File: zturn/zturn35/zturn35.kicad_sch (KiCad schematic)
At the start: 58 parts, among them U1 74AXP4T245, U10 74AXP4T245, U11 74AXP4T245, U12 74AXP4T245, U2 74AXP4T245, U3 74AXP4T245, U4 74AXP4T245, U5 74AXP4T245, U6 74AXP4T245, U7 74AXP4T245, U8 74AXP4T245, U9 74AXP4T245

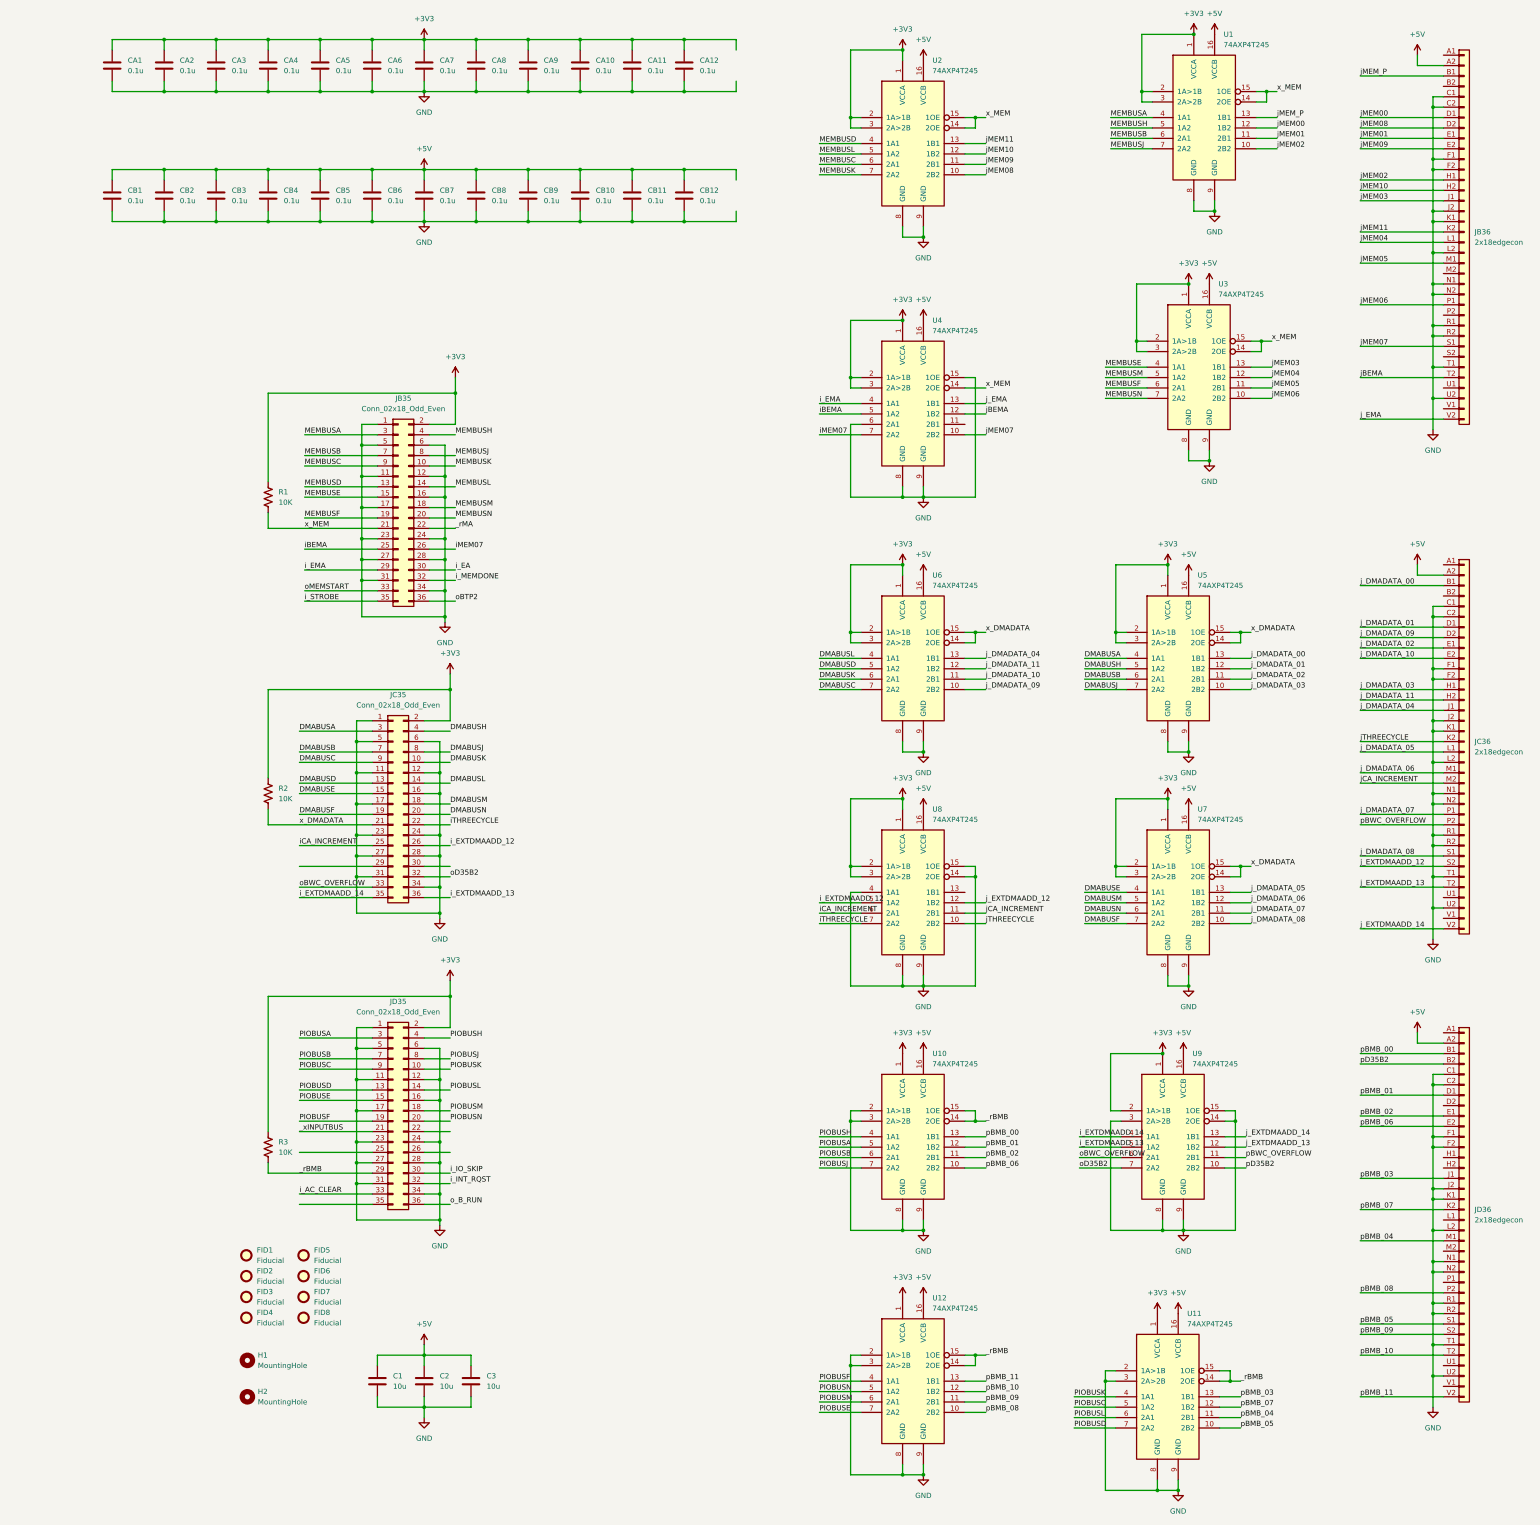
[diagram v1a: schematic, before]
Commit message: use transistors for bus drivers instead of chips
to handle the 180 & 220-ohm pullups
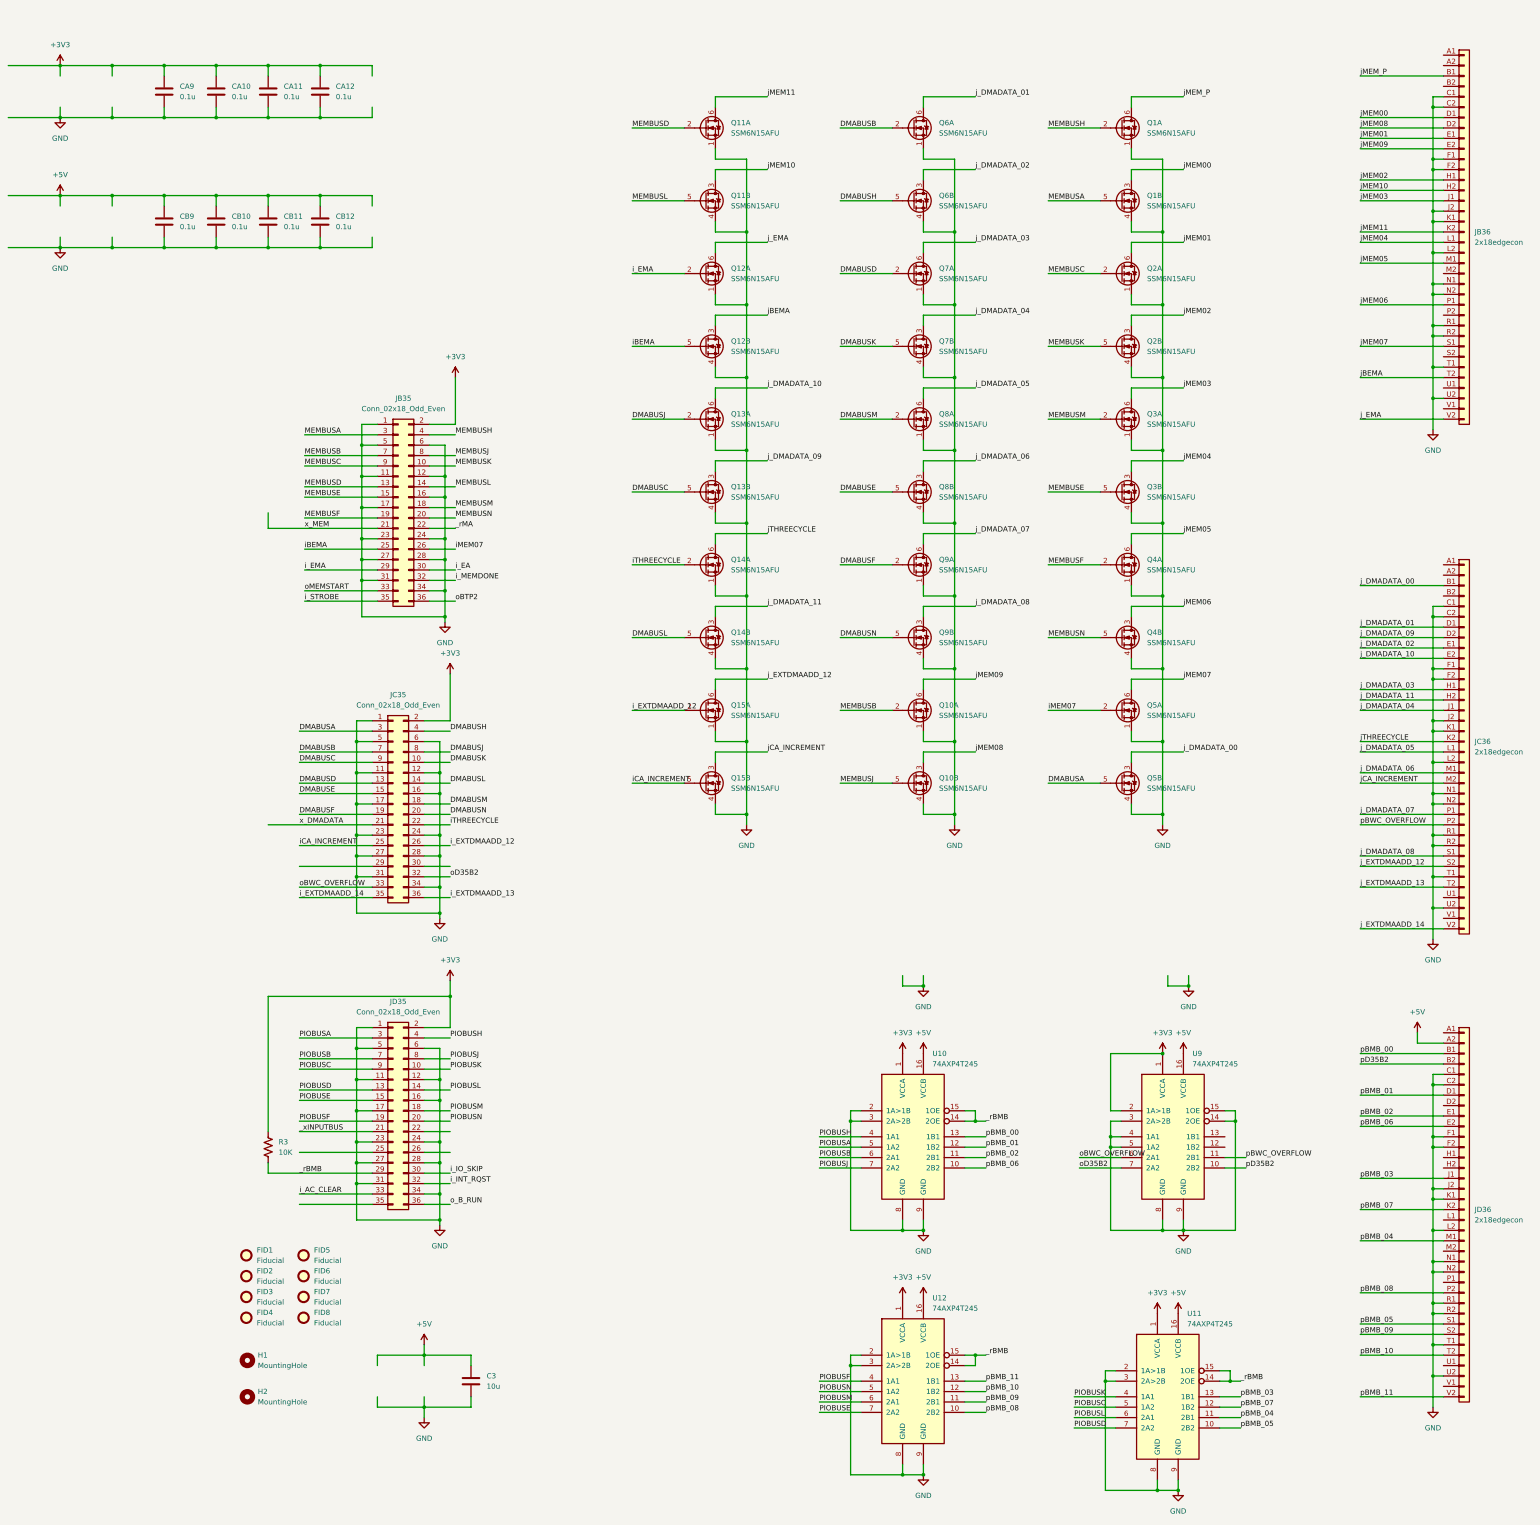
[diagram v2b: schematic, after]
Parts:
- removed C1, C2: 10u, Capacitor_SMD:C_1206_3216Metric, symbol Device:C
- removed CA1, CA2, CA3, CA4, CA5, CA6, CA7, CA8, CB1, CB2, CB3, CB4, CB5, CB6, CB7, CB8: 0.1u, Capacitor_SMD:C_0201_0603Metric, symbol Device:C
- removed R1, R2: 10K, Resistor_SMD:R_0201_0603Metric, symbol Device:R_US
- removed U1, U2, U3, U4, U5, U6, U7, U8: 74AXP4T245, Package_SO:TSSOP-16_4.4x5mm_P0.65mm, symbol mylibrary:74AXP4T245
- added Q1, Q10, Q11, Q12, Q13, Q14, Q15, Q2, Q3, Q4, Q5, Q6, Q7, Q8, Q9: SSM6N15AFU, Package_TO_SOT_SMD:SOT-363_SC-70-6, symbol mylibrary:SSM6N15AFU
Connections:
- net +5V: no longer JB36.A2, JC36.A2
- net DMABUSA: now also Q5.5 (G2)
- net DMABUSB: now also Q6.2 (G1)
- net DMABUSC: now also Q13.5 (G2)
- net DMABUSD: now also Q7.2 (G1)
- net DMABUSE: now also Q8.5 (G2)
- net DMABUSF: now also Q9.2 (G1)
- net DMABUSH: now also Q6.5 (G2)
- net DMABUSJ: now also Q13.2 (G1)
- net DMABUSK: now also Q7.5 (G2)
- net DMABUSL: now also Q14.5 (G2)
- net DMABUSM: now also Q8.2 (G1)
- net DMABUSN: now also Q9.5 (G2)
- net GND: now also U9.4 (1A1), U9.5 (1A2), Q1.1 (S1), Q1.4 (S2), Q10.1 (S1), Q10.4 (S2), Q11.1 (S1), Q11.4 (S2), Q12.1 (S1), Q12.4 (S2), Q13.1 (S1), Q13.4 (S2), Q14.1 (S1), Q14.4 (S2), Q15.1 (S1), Q15.4 (S2), Q2.1 (S1), Q2.4 (S2), Q3.1 (S1), Q3.4 (S2), Q4.1 (S1), Q4.4 (S2), Q5.1 (S1), Q5.4 (S2), Q6.1 (S1), Q6.4 (S2), Q7.1 (S1), Q7.4 (S2), Q8.1 (S1), Q8.4 (S2), Q9.1 (S1), Q9.4 (S2)
- net MEMBUSA: now also Q1.5 (G2)
- net MEMBUSB: now also Q10.2 (G1)
- net MEMBUSC: now also Q2.2 (G1)
- net MEMBUSD: now also Q11.2 (G1)
- net MEMBUSE: now also Q3.5 (G2)
- net MEMBUSF: now also Q4.2 (G1)
- net MEMBUSH: now also Q1.2 (G1)
- net MEMBUSJ: now also Q10.5 (G2)
- net MEMBUSK: now also Q2.5 (G2)
- net MEMBUSL: now also Q11.5 (G2)
- net MEMBUSM: now also Q3.2 (G1)
- net MEMBUSN: now also Q4.5 (G2)
- net iBEMA: now also Q12.5 (G2)
- net iCA_INCREMENT: now also Q15.5 (G2)
- net iMEM07: now also Q5.2 (G1)
- net iTHREECYCLE: now also Q14.2 (G1)
- net i_EMA: now also Q12.2 (G1)
- net i_EXTDMAADD_12: now also Q15.2 (G1)
- net i_EXTDMAADD_13: no longer U9.5 (1A2)
- net i_EXTDMAADD_14: no longer U9.4 (1A1)
- net jBEMA: now also Q12.3 (D2)
- net jCA_INCREMENT: now also Q15.3 (D2)
- net jMEM00: now also Q1.3 (D2)
- net jMEM01: now also Q2.6 (D1)
- net jMEM02: now also Q2.3 (D2)
- net jMEM03: now also Q3.6 (D1)
- net jMEM04: now also Q3.3 (D2)
- net jMEM05: now also Q4.6 (D1)
- net jMEM06: now also Q4.3 (D2)
- net jMEM07: now also Q5.6 (D1)
- net jMEM08: now also Q10.3 (D2)
- net jMEM09: now also Q10.6 (D1)
- net jMEM10: now also Q11.3 (D2)
- net jMEM11: now also Q11.6 (D1)
- net jMEM_P: now also Q1.6 (D1)
- net jTHREECYCLE: now also Q14.6 (D1)
- net j_DMADATA_00: now also Q5.3 (D2)
- net j_DMADATA_01: now also Q6.6 (D1)
- net j_DMADATA_02: now also Q6.3 (D2)
- net j_DMADATA_03: now also Q7.6 (D1)
- net j_DMADATA_04: now also Q7.3 (D2)
- net j_DMADATA_05: now also Q8.6 (D1)
- net j_DMADATA_06: now also Q8.3 (D2)
- net j_DMADATA_07: now also Q9.6 (D1)
- net j_DMADATA_08: now also Q9.3 (D2)
- net j_DMADATA_09: now also Q13.3 (D2)
- net j_DMADATA_10: now also Q13.6 (D1)
- net j_DMADATA_11: now also Q14.3 (D2)
- net j_EMA: now also Q12.6 (D1)
- net j_EXTDMAADD_12: now also Q15.6 (D1)
- net j_EXTDMAADD_13: no longer U9.12 (1B2)
- net j_EXTDMAADD_14: no longer U9.13 (1B1)
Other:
- moved on the sheet: CA10, CA11, CA12, CA9, CB10, CB11, CB12, CB9
